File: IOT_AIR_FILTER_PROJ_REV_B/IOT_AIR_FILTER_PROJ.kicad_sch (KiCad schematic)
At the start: 72 parts, among them J10 Conn_01x05_Socket, J2 Conn_01x02_Socket, J3 Conn_02x20_Odd_Even, J4 Conn_01x04_Pin, J5 Conn_01x04_Pin, J6 Conn_01x04_Pin, J7 Conn_01x04_Pin, J8 Conn_01x04_Pin, J9 Conn_01x04_Pin, U1 AMS1117-5.0, U2 TXS0102DCT, U3 PIC16F18156T-I/SO, U4 MC14051BDR2G, U5 INA180A2, U6 INA180A2, U7 INA180A2, U8 INA180A2, U9 MCP23008-xSO, Y1 Crystal_GND24

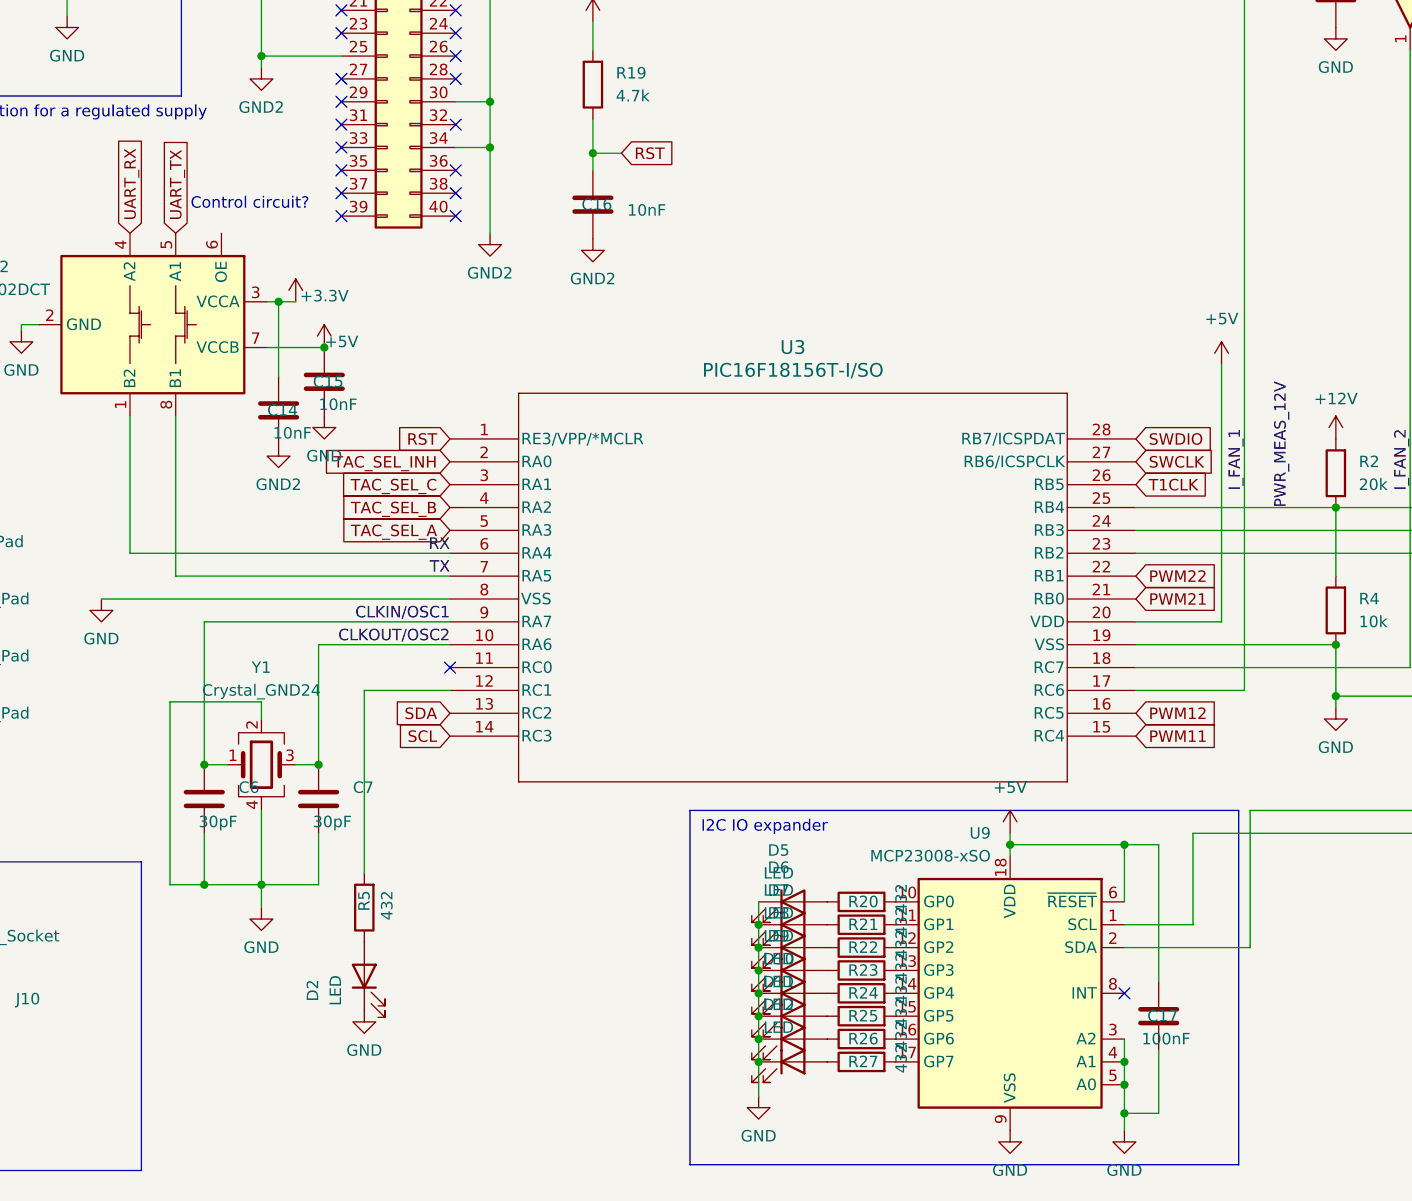
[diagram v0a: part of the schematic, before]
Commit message: replaced i2c expander with dedicated LED controller
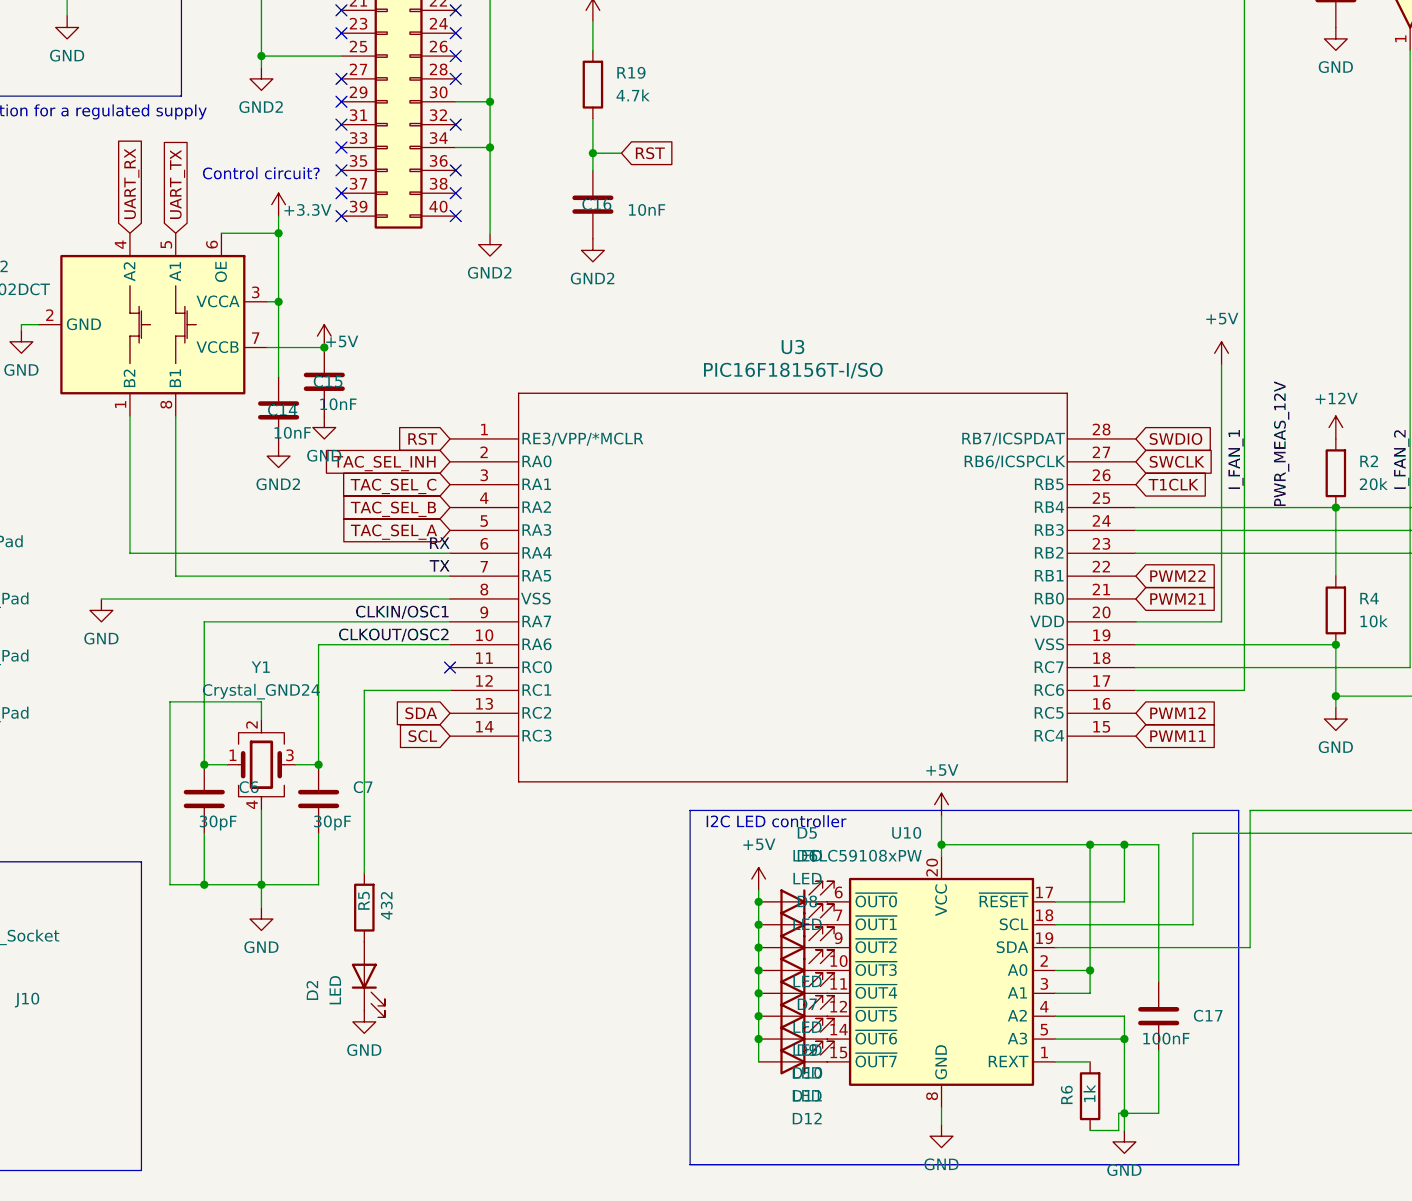
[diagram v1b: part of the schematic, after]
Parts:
- removed R20, R21, R22, R23, R24, R25, R26, R27: 432, Resistor_SMD:R_0402_1005Metric, symbol Device:R
- removed U9: MCP23008-xSO, Package_SO:SOIC-18W_7.5x11.6mm_P1.27mm, symbol Interface_Expansion:MCP23008-xSO
- added R6: 1k, Resistor_SMD:R_1210_3225Metric, symbol Device:R
- added U10: TLC59108xPW, Package_SO:TSSOP-20_4.4x6.5mm_P0.65mm, symbol Driver_LED:TLC59108xPW
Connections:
- net +3.3V: now also U2.6 (OE)
- net +5V: now also D10.2 (A), D11.2 (A), D12.2 (A), D5.2 (A), D6.2 (A), D7.2 (A), D8.2 (A), D9.2 (A), U10.17 (~{RESET}), U10.2 (A0), U10.20 (VCC), U10.3 (A1)
- net GND: now also R6.1, U10.13 (GND), U10.16 (GND), U10.4 (A2), U10.5 (A3), U10.8 (GND); no longer D10.1 (K), D11.1 (K), D12.1 (K), D5.1 (K), D6.1 (K), D7.1 (K), D8.1 (K), D9.1 (K)
- net SCL: now also U10.18 (SCL)
- net SDA: now also U10.19 (SDA)
- new net: D7.1 (K), U10.9 (~{OUT2})
- new net: D5.1 (K), U10.6 (~{OUT0})
- new net: D10.1 (K), U10.12 (~{OUT5})
- new net: D6.1 (K), U10.7 (~{OUT1})
- new net: D8.1 (K), U10.10 (~{OUT3})
- new net: R6.2, U10.1 (REXT)
- new net: D11.1 (K), U10.14 (~{OUT6})
- new net: D9.1 (K), U10.11 (~{OUT4})
- new net: D12.1 (K), U10.15 (~{OUT7})
- no-connect marks 35 -> 34
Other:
- note added: "I2C LED controller"
- note removed: "I2C IO expander"
- moved on the sheet: D10, D11, D12, D5, D6, D7, D8, D9
